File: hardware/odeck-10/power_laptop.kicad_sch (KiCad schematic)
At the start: 128 parts, among them Q201 BSC0805LS, Q202 BSC0805LS, Q203 CSD18543Q3A, Q204 CSD18543Q3A, Q205 AO3400A, Q206 AO3400A, Q207 AO3400A, Q208 AO3400A, Q209 AO3400A, Q210 AO3400A, Q211 AO3400A, Q212 2N7002, Q213 BSC040N08NS5, Q214 BSC040N08NS5, Q215 CSD18543Q3A, Q216 AO3400A, Q217 AO3400A, Q218 AO3400A, U201 LM51770, U202 LM74800-Q1, U203 SN74LVC1G11, U204 INA226, U205 LM74502, U206 TPS259470A, U207 TLV3011

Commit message: Schematic review + footprint verification; fix all MAJOR findings
Reviews (docs/review/): power, PD/mux, data path, MCU/UI - 0 blockers,
7 majors, all resolved:
- power: diode-OR inputs (no shutdown-based PD-in priority), sink hand-over
  gated by delayed PG_5V, PD-in capacitance within 100 uF, HV resistor sizes,
  OVP filter/threshold, VBB_PG soft-start qualification
- card reader MS2_INS/SD2_WP phantom card, hub VBUS_DET level buffer
- RP2350 inductor dot text; minors across all sheets (HPD pull-down, PMG1
  INT pin, PHY TX caps, erratum E9 pull-downs, PHY I2C bridge gating,
  backlight 39 ohm, +1V1 cap, IOX P7)
Footprints: all 54 custom footprints checked vs manufacturer drawings,
50 fixed (courtyards, pads, paste, RJ45 mirrored pinout, EP sizes, holes);
removed obsolete FL_001 placeholder.
Firmware rules collected in docs/design/mcu.md.
186 parts, all JLC stock >= 5; netlist verify OK; ERC clean.

Co-Authored-By: Claude Opus 5.5 <noreply@anthropic.com>
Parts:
- added C244: 100n, Capacitor_SMD:C_0402_1005Metric, symbol Device:C
- added D205: BAV70, Package_TO_SOT_SMD:SOT-23, symbol Diode:BAV70
- added D206: 1N4148W, Diode_SMD:D_SOD-123, symbol Device:D
- added Q219, Q220, Q221: AO3400A, Package_TO_SOT_SMD:SOT-23, symbol Transistor_FET:AO3400A
- added R256, R258: 10k, Resistor_SMD:R_0402_1005Metric, symbol Device:R
- added R257: 4.7k, Resistor_SMD:R_0402_1005Metric, symbol Device:R
- C205: value 47u/100V -> 10u/50V; footprint Capacitor_SMD:CP_Elec_10x10 -> Capacitor_SMD:C_1210_3225Metric; symbol Device:C_Polarized -> Device:C; LCSC C371305 -> C432929
- C211: value 10u/50V -> 100u/35V; footprint Capacitor_SMD:C_1210_3225Metric -> Capacitor_SMD:CP_Elec_6.3x7.7; symbol Device:C -> Device:C_Polarized; LCSC C432929 -> C2982822
- C213: value 100u/35V -> 100n/50V; footprint Capacitor_SMD:CP_Elec_6.3x7.7 -> Capacitor_SMD:C_0603_1608Metric; symbol Device:C_Polarized -> Device:C; LCSC C2982822 -> C14663
- C214: value 100n/50V -> 100n/100V; LCSC C14663 -> C15725
- C215: value 100n/100V -> 1u/100V; footprint Capacitor_SMD:C_0603_1608Metric -> Capacitor_SMD:C_0805_2012Metric; LCSC C15725 -> C126585
- C216: value 1u/100V -> 1u/50V; footprint Capacitor_SMD:C_0805_2012Metric -> Capacitor_SMD:C_0603_1608Metric; LCSC C126585 -> C15849
- C217: value 1u/50V -> 22u; footprint Capacitor_SMD:C_0603_1608Metric -> Capacitor_SMD:C_0805_2012Metric; LCSC C15849 -> C45783
- C219: value 22u -> 100n/50V; footprint Capacitor_SMD:C_0805_2012Metric -> Capacitor_SMD:C_0603_1608Metric; LCSC C45783 -> C14663
- C221: value 100n/50V -> 100p; footprint Capacitor_SMD:C_0603_1608Metric -> Capacitor_SMD:C_0402_1005Metric; LCSC C14663 -> C1546
- C222: value 100p -> 22n; LCSC C1546 -> C1532
- C223: value 22n -> 6.8n; LCSC C1532 -> C1542
- C224: value 6.8n -> 82p; LCSC C1542 -> C45501
- C225: value 82p -> 1n; LCSC C45501 -> C1523
- C226: value 1n -> 4.7u; footprint Capacitor_SMD:C_0402_1005Metric -> Capacitor_SMD:C_0603_1608Metric; LCSC C1523 -> C19666
- C227: value 4.7u -> 4.7n; footprint Capacitor_SMD:C_0603_1608Metric -> Capacitor_SMD:C_0402_1005Metric; LCSC C19666 -> C1538
- C242: value 470p -> 100n; LCSC C1537 -> C1525
- C243: value 100n -> 2.2n; LCSC C1525 -> C1531
- D201: value BZT52C5V1 -> 1N4148W; symbol Device:D_Zener -> Device:D; LCSC C173407 -> C81598
- D202: value BAT54A -> BZT52C5V1; footprint Package_TO_SOT_SMD:SOT-23 -> Diode_SMD:D_SOD-123; symbol Diode:BAT54A -> Device:D_Zener; LCSC C130910 -> C173407
- D203: value BAV70 -> BAT54A; symbol Diode:BAV70 -> Diode:BAT54A; LCSC C68978 -> C130910
- D204: value 1N4148W -> BAT46W; symbol Device:D -> Device:D_Schottky; LCSC C81598 -> C83152
- Q215: value CSD18543Q3A -> AO3400A; footprint odeck:VSONP-8_L3.1-W3.1-P0.65-LS3.5-BL -> Package_TO_SOT_SMD:SOT-23; symbol odeck:CSD18543Q3A -> Transistor_FET:AO3400A; LCSC C840100 -> C20917; MPN CSD18543Q3A -> (none)
- Q217: value AO3400A -> CSD18543Q3A; footprint Package_TO_SOT_SMD:SOT-23 -> odeck:VSONP-8_L3.1-W3.1-P0.65-LS3.5-BL; symbol Transistor_FET:AO3400A -> odeck:CSD18543Q3A; LCSC C20917 -> C840100; MPN (none) -> CSD18543Q3A
- R233: value 470k -> 1M; footprint Resistor_SMD:R_0805_2012Metric -> Resistor_SMD:R_0402_1005Metric; LCSC C17709 -> C26083
- R234: value 150 -> 470k; footprint Resistor_SMD:R_2512_6332Metric -> Resistor_SMD:R_0805_2012Metric; LCSC C2934049 -> C17709
- R235: value 255k -> 150; footprint Resistor_SMD:R_0402_1005Metric -> Resistor_SMD:R_2512_6332Metric; LCSC C270623 -> C2934049
- R236: value 10k -> 255k; LCSC C25744 -> C270623
- R237: value 100 -> 10k; LCSC C25076 -> C25744
- R238: value 100k -> 100; LCSC C25741 -> C25076
- R239: value 10k -> 100k; LCSC C25744 -> C25741
- R240: value 100k -> 10k; LCSC C25741 -> C25744
- R241: value 5m -> 100k; footprint Resistor_SMD:R_2512_6332Metric -> Resistor_SMD:R_0402_1005Metric; LCSC C844900 -> C25741; MPN WSL25125L000FEA -> (none)
- R242: value 422k -> 100k; LCSC C477738 -> C25741
- R243: value 100k -> 5m; footprint Resistor_SMD:R_0402_1005Metric -> Resistor_SMD:R_2512_6332Metric; LCSC C25741 -> C844900; MPN (none) -> WSL25125L000FEA
- R244: value 121k -> 422k; LCSC C11693 -> C477738
- R245: value 47k -> 100k; LCSC C25792 -> C25741
- R246: value 40.2k -> 121k; LCSC C25893 -> C11693
- R247, R253: value 10k -> 47k; LCSC C25744 -> C25792
- R248: value 1k -> 40.2k; LCSC C11702 -> C25893
- R250: value 47k -> 1k; LCSC C25792 -> C11702
- R251: value 1.1M -> 100k; LCSC C133039 -> C25741
- R252: value 47k -> 10k; LCSC C25792 -> C25744
- R254: value 4.7k -> 1.1M; LCSC C25900 -> C133039
- R255: value 10k -> 46.4k; LCSC C25744 -> C5126026
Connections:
- net +3V3: now also R240.2, R242.2, C244.1, R258.2; no longer C243.1, R239.2, R255.2
- net BB_BIAS: now also C216.1; no longer C217.1
- net BB_COMP: now also C224.1; no longer C225.1
- net BB_COMPZ: now also C223.1; no longer C224.1
- net BB_CSA: now also C221.1; no longer C222.1
- net BB_CSB: now also C221.2; no longer C222.2
- net BB_DIS: now also R235.2; no longer R234.2
- net BB_ENKILL: now also D201.2 (A), D202.1 (K), R234.2; no longer D201.1 (K), Q208.1 (G)
- net BB_FBM: now also C226.1; no longer C227.1
- net BB_HB1: now also C219.1; no longer C220.1
- net BB_HB2: now also C220.1; no longer C221.1
- net BB_IMONZ: now also C225.1; no longer C226.1
- net BB_PSO: now also C205.1; no longer C209.1
- net BB_SS: now also C222.1; no longer C223.1
- net BB_SW1: now also C219.2; no longer C220.2
- net BB_SW2: now also C220.2; no longer C221.2
- net BB_VCC: now also C217.1; no longer C219.1
- net EXT_PWR_PRESENT: now also Q218.1 (G); no longer Q216.1 (G)
- net GND: now also C222.2, D202.2 (A), Q215.2 (S), R237.2, R239.2, R241.2, R249.2, R253.2, R255.2, C244.2, Q219.2 (S), Q220.2 (S), Q221.2 (S); no longer C219.2, D201.2 (A), Q217.2 (S), Q218.2 (S), R236.2, R238.2, R240.2, R243.2, R248.2, R252.2
- net LAPTOP_OVP_N: now also D203.2, Q221.3 (D), R258.1; no longer D202.2, Q218.3 (D), R255.1
- net LAPTOP_SNK_EN: now also R252.1; no longer R249.1
- net LAPTOP_SRC_EN: now also R241.1; no longer R240.1
- net OVP_DIV: now also C243.1, R255.1, R257.2; no longer C242.1, R251.2, R252.1
- net OVP_FB: now also D206.1 (K), R257.1; no longer D204.1 (K), R254.1
- net OVP_TOP: now also R254.1, D205.3 (K); no longer D203.3 (K), R251.1
- net OVP_TRIP: now also D206.2 (A), Q221.1 (G), R256.1; no longer D204.2 (A), Q218.1 (G), R253.1
- net SNK_GATE: now also Q217.4 (G); no longer Q215.4 (G)
- net SNK_ILM: now also R250.1; no longer R248.1
- net SNK_MID: now also Q217.1 (S), Q217.2 (S), Q217.3 (S), R248.1; no longer Q215.1 (S), Q215.2 (S), Q215.3 (S), R244.1
- net SNK_ON: now also Q218.3 (D), R252.2, R253.1, Q220.3 (D); no longer Q216.3 (D), Q217.3 (D), R249.2, R250.1
- net SNK_OV: now also R244.2, R245.1; no longer R242.2, R243.1
- net SNK_OVLO: now also R248.2, R249.1; no longer R246.2, R247.1
- net SNK_UV: now also R246.2, R247.1; no longer R244.2, R245.1
- net SRC_DVDT: now also R238.2; no longer R237.2
- net SRC_HGATE: now also R238.1; no longer R237.1
- net SRC_ON: now also R239.1, Q220.1 (G); no longer Q217.1 (G), R238.1
- net SRC_OV: now also R236.2, R237.1; no longer R235.2, R236.1
- net SRC_OVT: now also R236.1; no longer R235.1
- net SRC_PGOK: now also D203.3, Q216.3 (D), R240.1; no longer D202.3, R239.1
- net VBB_EN: now also R256.2; no longer R253.2
- net VBB_OUT: now also C209.1, R235.1, D205.2 (A); no longer C214.1, D203.2 (A), R234.1
- net VBB_PG: now also D203.1; no longer D202.1
- net VBUS_LAPTOP: now also R243.2, D205.1 (A); no longer D203.1 (A), R241.2
- net VBUS_LSW: now also Q217.5 (D), Q217.6 (D), Q217.7 (D), Q217.8 (D), Q217.9 (D), R243.1, R244.1; no longer Q215.5 (D), Q215.6 (D), Q215.7 (D), Q215.8 (D), Q215.9 (D), R241.1, R242.1
- net VIN: now also C214.1, R234.1; no longer C205.1, C216.1, R233.1
- new net BB_PGH: C227.1, D201.1 (K), Q208.1 (G), R233.1
- new net PG_5V: D204.1 (K), R251.1
- new net SNK_KX: Q218.2 (S), Q219.3 (D)
- new net SNK_PGD: C242.1, D204.2 (A), Q215.1 (G), Q219.1 (G), R251.2
- new net SRC_PG5N: Q215.3 (D), Q216.1 (G), R242.1
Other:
- note added: "4. LAPTOP SOURCE SWITCH VBB_OUT -> VBUS_LSW -> 5 mOhm -> VBUS_LAPTOP LM74800-Q1: Q (DGATE) = ideal diode (blocks laptop -> VBB_OUT in < 1 us), Q (HGATE) = on/off, common drain, 2x BSC040N08NS5 (80 V, 4 mOhm @10 V): 5 A -> 0.26 W total. HARDWARE ENABLE: SRC_ON = LAPTOP_SRC_EN AND EXT_PWR_PRESENT AND (VBB_PG AND LAPTOP_OVP_N AND PG5_DLY) 74LVC1G11 3-input AND; VBB_PG and LAPTOP_OVP_N (both open-dra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"
- note added: "7. INDEPENDENT VBUS OVP (latched) -> LAPTOP_OVP_N Senses max(VBUS_LAPTOP, VBB_OUT) through BAV70 (100 V): also catches a run-away buck-boost before the source switch closes. 1.1M/46.4k + 0.45 V diode: trip = 1.242 x 24.7 + 0.45 = 31.1 V (~29.9-32.3 V RSS, 29.3-33.1 V all corners) > 28.7 V max regulation; 2.2 nF -> 98 us filter: a 5 A laptop unplug at 28 V (~1.2 V overshoot) reaches the comparator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"
- note removed: "4. LAPTOP SOURCE SWITCH VBB_OUT -> VBUS_LSW -> 5 mOhm -> VBUS_LAPTOP LM74800-Q1: Q (DGATE) = ideal diode (blocks laptop -> VBB_OUT in < 1 us), Q (HGATE) = on/off, common drain, 2x BSC040N08NS5 (80 V, 4 mOhm @10 V): 5 A -> 0.26 W total. HARDWARE ENABLE: SRC_ON = LAPTOP_SRC_EN AND EXT_PWR_PRESENT AND (VBB_PG AND LAPTOP_OVP_N) 74LVC1G11 3-input AND; VBB_PG and LAPTOP_OVP_N (both open-drain, 10k pull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"
- note removed: "7. INDEPENDENT VBUS OVP (latched) -> LAPTOP_OVP_N Senses max(VBUS_LAPTOP, VBB_OUT) through BAV70 (100 V): also catches a run-away buck-boost before the source switch closes. 1.1M/47k + 0.45 V diode: trip = 1.242 x 24.4 + 0.45 = 30.8 V (29.6-32.0 V incl. 1 % ref, 15 mV offset, 1 % R) > 28.7 V max regulation; 470 pF -> 21 us filter. TLV3011 (open-drain, internal 1.242 V ref): output pulled up to VB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"
- moved on the sheet: C206, C207, C208, C209, C210, C212, C214, C215, C216, C217, C218, C219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

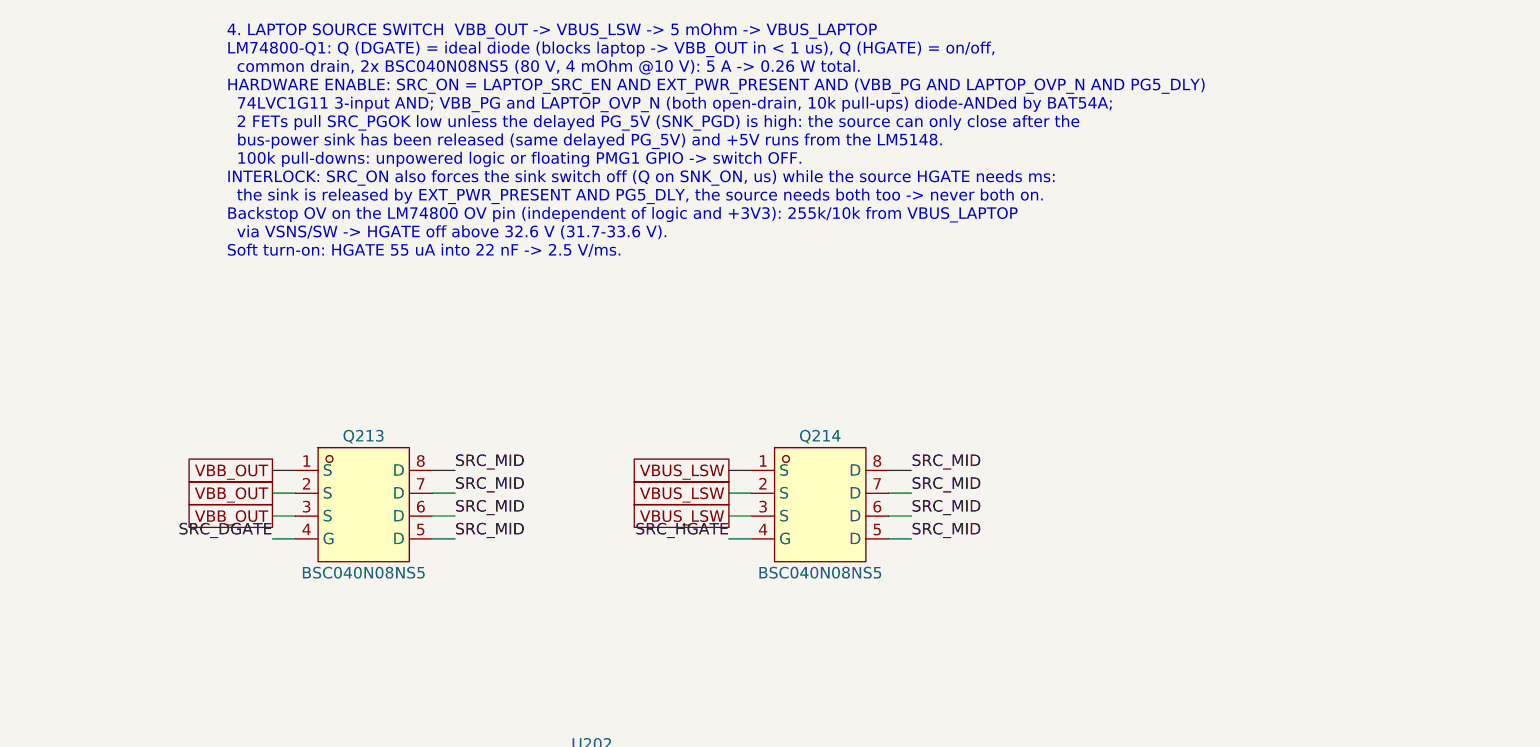
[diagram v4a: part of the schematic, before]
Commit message: Cost pass, PCB sync + rough placement, renders, README
- cost pass: extended parts 129 -> 114 (~$45/order less), nets unchanged
- tools/pcbsync.py: scripted update-PCB-from-schematic (keeps placed parts)
- tools/set_outline.py; board grown to 130x85 mm (provisional)
- hardware/odeck-10/placement.py: edge connectors + anchor-based packing,
  small passives spill to bottom; all 796 parts on the board (2 at anchor)
- docs/images: top/bottom/iso renders of the rough placement
- README.md: overview, architecture, repo layout, workflow, roadmap

Co-Authored-By: Claude Opus 5.5 <noreply@anthropic.com>
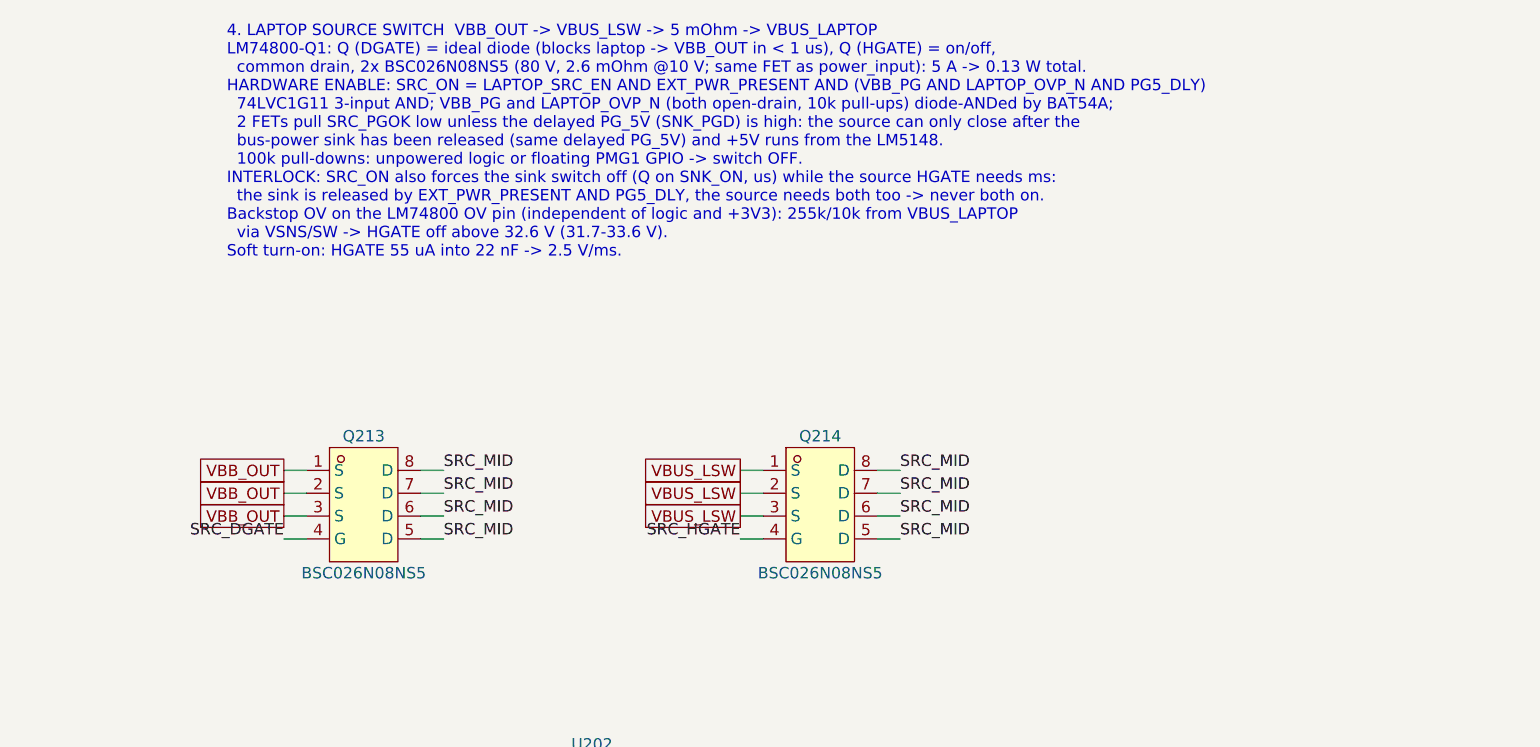
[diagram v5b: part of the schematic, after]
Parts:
- C214: footprint Capacitor_SMD:C_0603_1608Metric -> Capacitor_SMD:C_0805_2012Metric; LCSC C15725 -> C28233
- C223: footprint Capacitor_SMD:C_0402_1005Metric -> Capacitor_SMD:C_0603_1608Metric; LCSC C1542 -> C1631
- C239: footprint Capacitor_SMD:C_0402_1005Metric -> Capacitor_SMD:C_0603_1608Metric; LCSC C1536 -> C1613
- C243: footprint Capacitor_SMD:C_0402_1005Metric -> Capacitor_SMD:C_0603_1608Metric; LCSC C1531 -> C1604
- Q213, Q214: value BSC040N08NS5 -> BSC026N08NS5; footprint odeck:PG-TDSON-8_L5.9-W5.1-P1.27-LS6.2-BL -> odeck:PG-TDSON-8_L5.0-W6.0-P1.27-BL-EP; symbol odeck:BSC040N08NS5 -> odeck:BSC026N08NS5ATMA1; LCSC C534333 -> C5955453; MPN BSC040N08NS5 -> BSC026N08NS5ATMA1
- R201: LCSC C844693 -> C459681; MPN WSL25124L000FEA -> RLP25FEGR004
- R243: footprint Resistor_SMD:R_2512_6332Metric -> Resistor_SMD:R_1206_3216Metric; LCSC C844900 -> C316225; MPN WSL25125L000FEA -> RLM12FTCMR005
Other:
- note added: "4. LAPTOP SOURCE SWITCH VBB_OUT -> VBUS_LSW -> 5 mOhm -> VBUS_LAPTOP LM74800-Q1: Q (DGATE) = ideal diode (blocks laptop -> VBB_OUT in < 1 us), Q (HGATE) = on/off, common drain, 2x BSC026N08NS5 (80 V, 2.6 mOhm @10 V; same FET as power_input): 5 A -> 0.13 W total. HARDWARE ENABLE: SRC_ON = LAPTOP_SRC_EN AND EXT_PWR_PRESENT AND (VBB_PG AND LAPTOP_OVP_N AND PG5_DLY) 74LVC1G11 3-input AND; VBB_PG and 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"
- note removed: "4. LAPTOP SOURCE SWITCH VBB_OUT -> VBUS_LSW -> 5 mOhm -> VBUS_LAPTOP LM74800-Q1: Q (DGATE) = ideal diode (blocks laptop -> VBB_OUT in < 1 us), Q (HGATE) = on/off, common drain, 2x BSC040N08NS5 (80 V, 4 mOhm @10 V): 5 A -> 0.26 W total. HARDWARE ENABLE: SRC_ON = LAPTOP_SRC_EN AND EXT_PWR_PRESENT AND (VBB_PG AND LAPTOP_OVP_N AND PG5_DLY) 74LVC1G11 3-input AND; VBB_PG and LAPTOP_OVP_N (both open-dra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"
